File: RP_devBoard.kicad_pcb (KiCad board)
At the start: 2 copper layers, 70 parts, among them J1 Conn_01x04, J2 Conn_01x04, J3 TC2030, J4 TC2030, J5 USB_C_Receptacle, J6 USB_C_Receptacle, U1 RP2350B, U10 USBLC6-2SC6, U11 USBLC6-2SC6, U2 ESP32-C3-WROOM-02, U3 BME280, U4 TPS628502, U5 W25Q128JVS, U6 W25Q128JVS, U7 MAX40200AUK, U8 MAX40200AUK, U9 MAX40200AUK, Y1 12MHz

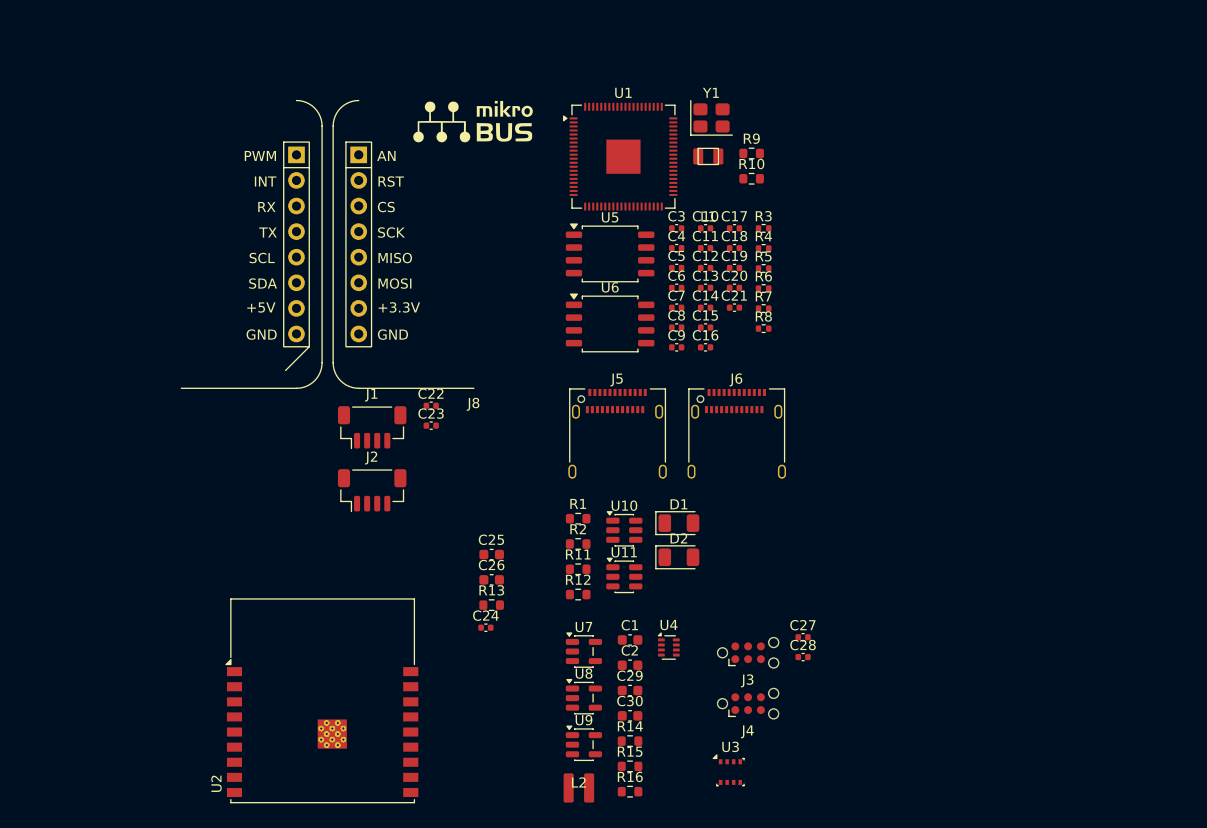
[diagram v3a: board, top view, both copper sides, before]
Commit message: correction of mikroBUS, USB on ESP32 and power mosfet
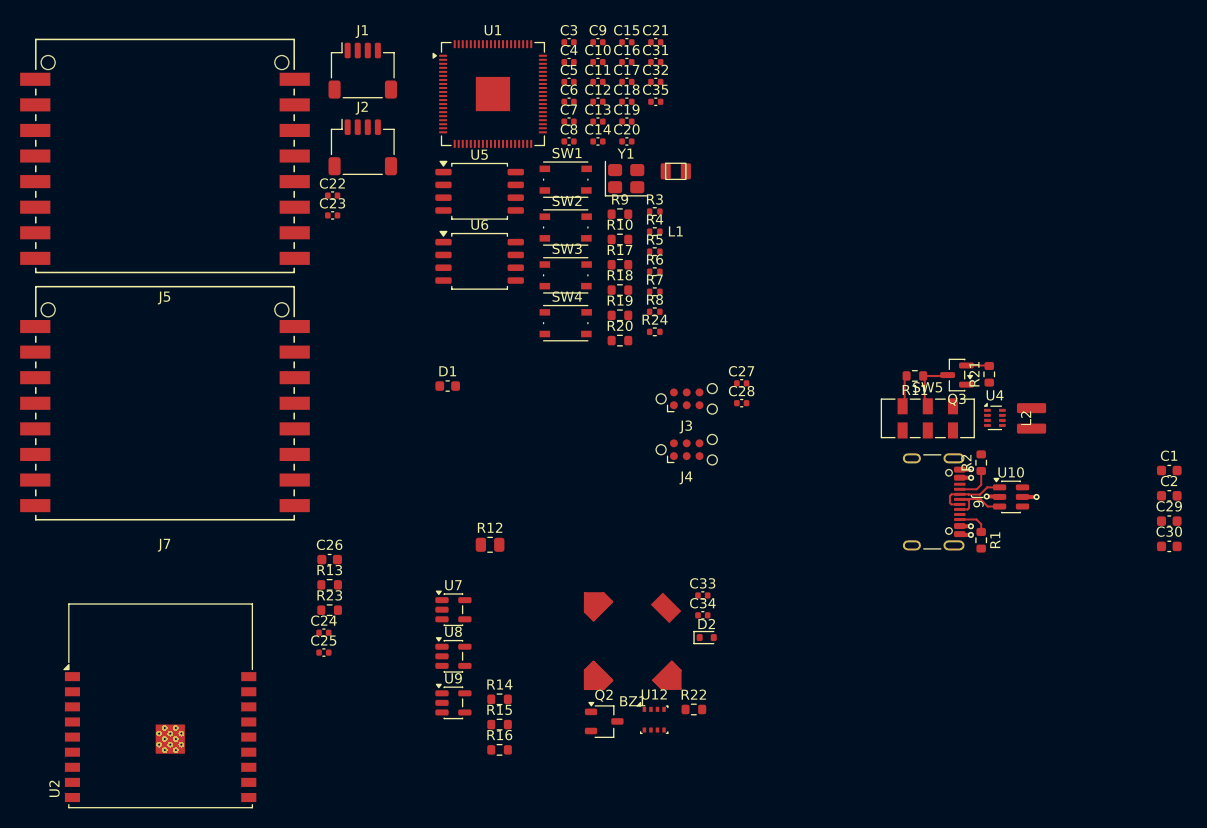
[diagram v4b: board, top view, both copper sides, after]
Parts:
- removed J8: ~, Sadman_connectors:MikroBUS_Left
- removed J9: ~, Sadman_connectors:MikroBUS_Right
- removed U11: USBLC6-2SC6, Package_TO_SOT_SMD:SOT-23-6
- removed U3: BME280, Package_LGA:Bosch_LGA-8_2.5x2.5mm_P0.65mm_ClockwisePinNumbering
- added BZ1: Buzzer, Sadman_audio:SMT-0827-S-HT-R, F.Cu at (99.0, 101.0)
- added C31: 100nF, Capacitor_SMD:C_0402_1005Metric, F.Cu at (101.3, 43.5)
- added C32: 100nF, Capacitor_SMD:C_0402_1005Metric, F.Cu at (101.3, 45.5)
- added C33: 100nF, Capacitor_SMD:C_0402_1005Metric, F.Cu at (106.0, 96.5)
- added C34: 100nF, Capacitor_SMD:C_0402_1005Metric, F.Cu at (106.0, 98.5)
- added C35: 100nF, Capacitor_SMD:C_0402_1005Metric, F.Cu at (101.3, 47.5)
- added J7: Conn_02x08_Counter_Clockwise, Sadman_connectors:CONN2X8_MIKROE-4248_MKE, F.Cu at (52.6, 77.4)
- added Q2: AO3400A, Package_TO_SOT_SMD:TSOT-23, F.Cu at (96.2, 109.0)
- added Q3: AO3401A, Package_TO_SOT_SMD:SOT-23, F.Cu at (131.2, 74.6)
- added R17: 2.2K, Resistor_SMD:R_0603_1608Metric, F.Cu at (97.7, 63.6)
- added R18: 2.2K, Resistor_SMD:R_0603_1608Metric, F.Cu at (97.7, 66.2)
- added R19: 10k, Resistor_SMD:R_0603_1608Metric, F.Cu at (97.7, 68.7)
- added R20: 10k, Resistor_SMD:R_0603_1608Metric, F.Cu at (97.7, 71.2)
- added R21: 10k, Resistor_SMD:R_0603_1608Metric, F.Cu at (134.4, 74.5)
- added R22: 10k, Resistor_SMD:R_0603_1608Metric, F.Cu at (105.1, 107.8)
- added R23: 10k, Resistor_SMD:R_0603_1608Metric, F.Cu at (68.9, 97.9)
- added R24: 1K, Resistor_SMD:R_0402_1005Metric, F.Cu at (101.2, 70.3)
- added SW1: SW_Push, Button_Switch_SMD:SW_Push_1P1T_NO_Vertical_Wuerth_434133025816, F.Cu at (92.4, 55.2)
- added SW2: SW_Push, Button_Switch_SMD:SW_Push_1P1T_NO_Vertical_Wuerth_434133025816, F.Cu at (92.4, 60.0)
- added SW3: SW_Push, Button_Switch_SMD:SW_Push_1P1T_NO_Vertical_Wuerth_434133025816, F.Cu at (92.4, 64.7)
- added SW4: SW_Push, Button_Switch_SMD:SW_Push_1P1T_NO_Vertical_Wuerth_434133025816, F.Cu at (92.4, 69.5)
- added SW5: SW, Button_Switch_SMD:SW_DPDT_CK_JS202011JCQN, F.Cu at (128.3, 78.9)
- added U12: BME280, Package_LGA:Bosch_LGA-8_2.5x2.5mm_P0.65mm_ClockwisePinNumbering, F.Cu at (101.1, 108.8)
- C25: value 1uF -> 100nF; footprint Capacitor_SMD:C_0603_1608Metric -> Capacitor_SMD:C_0402_1005Metric
- D1: value SD1206S040S2R0 -> LG; footprint Diode_SMD:D_1206_3216Metric -> Inductor_SMD:L_0603_1608Metric
- D2: value SD1206S040S2R0 -> 1N4148WT; footprint Diode_SMD:D_1206_3216Metric -> Diode_SMD:D_SOD-523
- J1, J2: footprint Connector_JST:JST_SH_BM04B-SRSS-TB_1x04-1MP_P1.00mm_Vertical -> Connector_JST:JST_SH_SM04B-SRSS-TB_1x04-1MP_P1.00mm_Horizontal
- J5: value USB_C_Receptacle -> Conn_02x08_Counter_Clockwise; footprint Connector_USB:USB_C_Receptacle_Amphenol_12401610E4-2A -> Sadman_connectors:CONN2X8_MIKROE-4248_MKE
- J6: footprint Connector_USB:USB_C_Receptacle_Amphenol_12401610E4-2A -> Connector_USB:USB_C_Receptacle_GCT_USB4105-xx-A_16P_TopMnt_Horizontal
- R11: value 5.1k -> 0
- R12: value 5.1k -> 200; footprint Resistor_SMD:R_0603_1608Metric -> Resistor_SMD:R_0805_2012Metric
- moved L2 58.0 mm to (138.6, 78.9), turned to 90 degrees
- moved C1 56.1 mm to (152.3, 84.1)
- moved C2 56.1 mm to (152.3, 86.6)
- moved C29 56.1 mm to (152.3, 89.1)
- moved C30 56.1 mm to (152.3, 91.6)
- moved J5 53.2 mm to (52.6, 52.8)
- moved R2 40.8 mm to (133.6, 83.3), turned to 90 degrees
- moved R1 40.1 mm to (133.6, 91.0), turned to -90 degrees
- moved U4 39.6 mm to (135.0, 78.8)
- moved R11 38.5 mm to (127.0, 74.7), turned to 180 degrees
- moved U10 38.5 mm to (136.6, 86.7)
- moved J1 35.4 mm to (72.2, 44.4)
- moved J2 34.1 mm to (72.2, 52.0)
- moved C9 31.3 mm to (95.6, 41.6)
- moved C15 29.4 mm to (98.4, 41.6)
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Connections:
- D1 pad 1: +5V -> GND
- D1 pad 2: VUSB1 -> Net-(D1-A)
- D2 pad 1: +5V -> +3V3
- D2 pad 2: VUSB0 -> Net-(BZ1--)
- R11 pad 1: Net-(J5-CC2) -> VUSB0
- R11 pad 2: GND -> Net-(Q3-G)
- R12 pad 1: Net-(J5-CC1) -> +5V
- R12 pad 2: GND -> Net-(D1-A)
- U1 pad 11: unconnected-(U1-GPIO12-Pad11) -> Net-(U1-GPIO12)
- U1 pad 25: unconnected-(U1-GPIO24-Pad25) -> /BZZ_PWM
- U1 pad 43: unconnected-(U1-GPIO34-Pad43) -> /RP_SS2
- U1 pad 77: /RP2350B/RPB_I2C_SDA -> /SDA
- U1 pad 78: /RP2350B/RPB_I2C_SCL -> /SCL
- U1 pad 9: unconnected-(U1-GPIO11-Pad9) -> Net-(U1-GPIO11)
- U10 pad 1: /USB_PORTS/USB0_DP -> /USB_PORTS/USB0_DN
- U10 pad 3: /USB_PORTS/USB0_DN -> /USB_PORTS/USB0_DP
- U10 pad 4: /USB0_DN -> /USB0_DP
- U10 pad 6: /USB0_DP -> /USB0_DN
- U2 pad 13: /USB1_DM -> unconnected-(U2-IO18-Pad13)
- U2 pad 14: /USB1_DP -> unconnected-(U2-IO19-Pad14)
- U2 pad 7: unconnected-(U2-IO8-Pad7) -> Net-(U2-IO8)
- U2 pad 8: unconnected-(U2-IO9-Pad8) -> /ESP_BOOT
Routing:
- net VUSB0: track 0.00 -> 9.42 mm, vias 0 -> 3
- net /USB_PORTS/USB0_DN: track 0.00 -> 7.03 mm
- net /USB_PORTS/USB0_DP: track 0.00 -> 6.94 mm
- net Net-(Q3-G): track 0.00 -> 5.99 mm
- net Net-(J6-CC1): track 0.00 -> 3.68 mm
- net GND: track 0.00 -> 3.58 mm, vias 0 -> 3
- net Net-(J6-CC2): track 0.00 -> 3.09 mm

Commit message: pcb power layout
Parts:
- added C36: 10uF, Capacitor_SMD:C_0603_1608Metric, F.Cu at (1.38, -148.4)
- added C37: 100nF, Capacitor_SMD:C_0402_1005Metric, F.Cu at (153.5, 88.6)
- added C38: 100nF, Capacitor_SMD:C_0402_1005Metric, F.Cu at (162.5, 94.0)
- added R25: 10k, Resistor_SMD:R_0603_1608Metric, F.Cu at (1.38, -145.9)
- C4, C6: footprint Capacitor_SMD:C_0402_1005Metric -> Capacitor_SMD:C_0603_1608Metric
- moved Q3 188.2 mm to (60.8, -99.9), turned to -90 degrees
- moved R11 187.6 mm to (55.8, -98.9)
- moved R21 187.3 mm to (64.0, -99.0)
- moved SW5 186.7 mm to (57.1, -93.7)
- moved BZ1 185.2 mm to (27.8, -69.9)
- moved C1 185.2 mm to (81.1, -86.8)
- moved C2 185.2 mm to (81.1, -84.3)
- moved C20 185.2 mm to (27.2, -119.5)
- moved C21 185.2 mm to (30.1, -129.4)
- moved C22 185.2 mm to (-1.98, -114.1)
- moved C23 185.2 mm to (-1.98, -112.2)
- moved C24 185.2 mm to (-2.85, -70.7)
- moved C25 185.2 mm to (-2.85, -68.8)
- moved C26 185.2 mm to (-2.28, -78.0)
- moved C27 185.2 mm to (38.6, -95.5)
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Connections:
- net Net-(U1-USB_DM) renamed /RP2350B/USB_IN_N
- net Net-(U1-USB_DP) renamed /RP2350B/USB_IN_P
- L1 pad 2: Net-(U1-VREG_LX) -> /RP2350B/VGREX_LX
- U1 pad 63: (no net) -> /RP2350B/VGREX_LX
- U2 pad 18: /ESP_BOOT -> unconnected-(U2-IO0-Pad18)
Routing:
- net +3V3: track 0.00 -> 24.4 mm, vias 0 -> 4
- net GND: track 3.58 -> 22.3 mm, vias 3 -> 24
- net +1V1: track 0.00 -> 12.2 mm, vias 0 -> 5
- net Net-(U1-XIN): track 0.00 -> 8.71 mm
- net Net-(Q3-G): track 5.99 -> 0.00 mm
- net VUSB0: track 9.42 -> 3.74 mm
- net /RP2350B/VGREX_LX: track 0.00 -> 5.32 mm
- net /RP2350B/USB_IN_P: track 0.00 -> 4.57 mm
- net /RP2350B/USB_IN_N: track 0.00 -> 4.56 mm
- net Net-(C19-Pad1): track 0.00 -> 4.06 mm
- net Net-(U1-VREG_AVDD): track 0.00 -> 4.01 mm
- net Net-(U1-XOUT): track 0.00 -> 1.81 mm
- net /USB0_DN: track 0.00 -> 1.74 mm
- net /USB0_DP: track 0.00 -> 1.60 mm
- added copper zone on F.Cu, net +1V1
- added copper zone on In2.Cu, net +1V1
- added copper zone on F.Cu, net /RP2350B/VGREX_LX
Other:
- copper layers 2 -> 4

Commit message: save
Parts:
- removed C21: 100nF, Capacitor_SMD:C_0402_1005Metric
- removed R10, R9: 0, Resistor_SMD:R_0603_1608Metric
- removed SW2: SW_Push, Button_Switch_SMD:SW_Push_1P1T_NO_Vertical_Wuerth_434133025816
- removed U6: W25Q128JVS, Package_SO:SOIC-8_5.3x5.3mm_P1.27mm
- added C39: 100nF, Capacitor_SMD:C_0402_1005Metric, F.Cu at (136.7, 110.7)
- added TP1: TestPoint, Connector_Pin:Pin_D1.0mm_L10.0mm, F.Cu at (89.3, 85.1)
- added TP10: TestPoint, TestPoint:TestPoint_THTPad_D1.0mm_Drill0.5mm, B.Cu at (180.7, 129.5)
- added TP11: TestPoint, TestPoint:TestPoint_THTPad_D1.0mm_Drill0.5mm, F.Cu at (103.9, 108.2)
- added TP12: TestPoint, TestPoint:TestPoint_THTPad_D1.0mm_Drill0.5mm, B.Cu at (99.0, 127.1)
- added TP13: TestPoint, TestPoint:TestPoint_THTPad_D1.0mm_Drill0.5mm, B.Cu at (99.0, 129.7)
- added TP14: TestPoint, TestPoint:TestPoint_THTPad_D1.0mm_Drill0.5mm, B.Cu at (99.0, 132.2)
- added TP15: TestPoint, TestPoint:TestPoint_THTPad_D1.0mm_Drill0.5mm, B.Cu at (99.0, 134.7)
- added TP16: TestPoint, TestPoint:TestPoint_THTPad_D1.0mm_Drill0.5mm, B.Cu at (99.0, 137.3)
- added TP17: TestPoint, TestPoint:TestPoint_THTPad_D1.0mm_Drill0.5mm, B.Cu at (99.0, 140.1)
- added TP18: TestPoint, TestPoint:TestPoint_THTPad_D1.0mm_Drill0.5mm, B.Cu at (121.8, 106.9)
- added TP19: TestPoint, TestPoint:TestPoint_Pad_D1.0mm, F.Cu at (133.1, 117.1)
- added TP2: TestPoint, Connector_Pin:Pin_D1.0mm_L10.0mm, F.Cu at (95.2, 90.4)
- added TP20: TestPoint, TestPoint:TestPoint_Pad_D1.0mm, F.Cu at (141.8, 115.4)
- added TP21: TestPoint, TestPoint:TestPoint_THTPad_D1.0mm_Drill0.5mm, F.Cu at (1.02, 1.02)
- added TP21: TestPoint, TestPoint:TestPoint_THTPad_D1.0mm_Drill0.5mm, B.Cu at (125.2, 93.2)
- added TP22: TestPoint, TestPoint:TestPoint_THTPad_D1.0mm_Drill0.5mm, F.Cu at (1.02, 4.08)
- added TP22: TestPoint, TestPoint:TestPoint_THTPad_D1.0mm_Drill0.5mm, B.Cu at (127.4, 93.2)
- added TP23: TestPoint, TestPoint:TestPoint_THTPad_D1.0mm_Drill0.5mm, B.Cu at (123.9, 106.9)
- added TP24: TestPoint, TestPoint:TestPoint_THTPad_D1.0mm_Drill0.5mm, B.Cu at (126.1, 106.9)
- added TP25: TestPoint, TestPoint:TestPoint_THTPad_D1.0mm_Drill0.5mm, F.Cu at (1.02, 7.12)
- added TP25: TestPoint, TestPoint:TestPoint_THTPad_D1.0mm_Drill0.5mm, B.Cu at (123.0, 93.2)
- added TP3: TestPoint, TestPoint:TestPoint_THTPad_D1.0mm_Drill0.5mm, B.Cu at (110.4, 92.5)
- added TP4: TestPoint, TestPoint:TestPoint_THTPad_D1.0mm_Drill0.5mm, B.Cu at (110.9, 112.0)
- added TP5: TestPoint, TestPoint:TestPoint_THTPad_D1.5mm_Drill0.7mm, F.Cu at (143.3, 92.7)
- added TP6: TestPoint, TestPoint:TestPoint_THTPad_D1.0mm_Drill0.5mm, B.Cu at (147.0, 97.1)
- added TP7: TestPoint, TestPoint:TestPoint_THTPad_D1.0mm_Drill0.5mm, B.Cu at (108.7, 104.9)
- added TP8: TestPoint, TestPoint:TestPoint_THTPad_D1.0mm_Drill0.5mm, B.Cu at (108.7, 102.6)
- added TP9: TestPoint, TestPoint:TestPoint_THTPad_D1.0mm_Drill0.5mm, B.Cu at (118.4, 100.0)
- C24: footprint Capacitor_SMD:C_0402_1005Metric -> Capacitor_SMD:C_0603_1608Metric
- D1: footprint Inductor_SMD:L_0603_1608Metric -> LED_SMD:LED_0805_2012Metric
- Q2: footprint Package_TO_SOT_SMD:TSOT-23 -> Package_TO_SOT_SMD:SOT-23
- R11: footprint Resistor_SMD:R_0603_1608Metric -> Resistor_SMD:R_0805_2012Metric
- SW5: footprint Button_Switch_SMD:SW_DPDT_CK_JS202011JCQN -> Button_Switch_SMD:SW_DIP_SPSTx01_Slide_6.7x4.1mm_W6.73mm_P2.54mm_LowProfile_JPin
- moved R25 419.6 mm to (28.5, 272.8)
- moved C31 377.1 mm to (176.8, 220.0)
- moved R19 368.8 mm to (169.3, 237.8)
- moved R20 368.8 mm to (169.3, 240.3)
- moved C32 367.4 mm to (179.6, 210.2)
- moved R24 364.1 mm to (172.8, 234.4)
- moved R8 357.0 mm to (151.6, 233.1)
- moved SW3 355.6 mm to (142.0, 228.2)
- moved SW4 355.6 mm to (142.0, 232.9)
- moved C25 347.1 mm to (27.9, 277.0)
- moved R13 344.6 mm to (28.5, 267.8)
- moved R23 344.6 mm to (28.5, 270.3)
- moved C22 342.1 mm to (28.8, 226.6)
- moved C23 342.1 mm to (28.8, 228.6)
- moved J2 309.7 mm to (163.0, 145.0)
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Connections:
- net Net-(U4-SW) renamed /POWER/SW_SOURCE
- J1 pad 3: /PERIPHERICS/RP_SDA -> /SDA
- J1 pad 4: /PERIPHERICS/RP_CLK -> /SCL
- J2 pad 3: /PERIPHERICS/RP_SDA -> /SDA
- J2 pad 4: /PERIPHERICS/RP_CLK -> /SCL
- Q2 pad 1: (no net) -> Net-(BZ1--)
- Q2 pad 2: (no net) -> /BZZ_PWM
- Q2 pad 3: (no net) -> GND
- R8 pad 2: /RP2350B/QSPI_SS -> Net-(U1-GPIO11)
- SW4 pad 1: Net-(U1-GPIO11) -> Net-(R8-Pad1)
- U5 pad 1: Net-(U5-~{CS}) -> /RP2350B/QSPI_SS
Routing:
- net /SCL: track 0.00 -> 166.5 mm, vias 0 -> 2
- net /SDA: track 0.00 -> 166.1 mm, vias 0 -> 2
- net /RP_CLK: track 0.00 -> 124.8 mm, vias 0 -> 2
- net /RP_MOSI: track 0.00 -> 109.8 mm, vias 0 -> 2
- net /RP_MISO: track 0.00 -> 91.3 mm, vias 0 -> 2
- net /USB0_DP: track 1.60 -> 43.8 mm, vias 0 -> 1
- net /USB0_DN: track 1.74 -> 43.8 mm, vias 0 -> 1
- net +3V3: track 24.4 -> 60.7 mm, vias 4 -> 29
- net /RP2350B/QSPI_SD0: track 0.00 -> 35.9 mm, vias 0 -> 1
- net /RP2350B/QSPI_SCLK: track 0.00 -> 33.9 mm, vias 0 -> 1
- net /RP2350B/QSPI_SD3: track 0.00 -> 29.6 mm, vias 0 -> 1
- net /RP2350B/QSPI_SD2: track 0.00 -> 25.6 mm, vias 0 -> 1
- net /RP2350B/QSPI_SD1: track 0.00 -> 25.4 mm, vias 0 -> 1
- net GND: track 22.3 -> 44.5 mm, vias 24 -> 47
- net /RP2350B/QSPI_SS: track 0.00 -> 21.1 mm, vias 0 -> 2
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- added copper zone on F.Cu, net +3V3
- added copper zone on F.Cu, net +3V3_TC1
- added copper zone on F.Cu, net +3V3_TC2
- added copper zone on F.Cu, net +3V3_USB
- added copper zone on F.Cu, net +5V
- added copper zone on F.Cu, net VUSB0
- removed copper zone on In2.Cu, net +1V1
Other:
- board outline added: 100 x 60 mm
